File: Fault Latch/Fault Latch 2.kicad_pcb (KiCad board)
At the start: 2 copper layers, 85 x 85 mm, 116 parts, among them J1 1053141312, J3 1053131202, J4 1053131202, J5 1053131202, K3 Fujitsu_FTR-LYCA005x, K5 Fujitsu_FTR-LYCA005x, K6 Fujitsu_FTR-LYCA005x, Q101 Q_NPN_BEC, Q102 Q_NPN_BEC, Q103 Q_NPN_BEC, Q104 Q_NPN_BEC, Q105 Q_NMOS_GSD, Q106 Q_NMOS_GSD, Q110 Q_NPN_BEC, Q111 Q_NPN_BEC, Q112 Q_NMOS_GSD, Q113 Q_NMOS_GSD, Q114 Q_NMOS_GSD, Q115 Q_NMOS_GSD, Q117 Q_NMOS_GSD, Q118 Q_NMOS_GSD, Q119 Q_NMOS_GSD, Q120 Q_NMOS_GSD, Q121 Q_NMOS_GSD, Q122 Q_NMOS_GSD, Q123 Q_NMOS_GSD, Q124 Q_NMOS_GSD, Q125 Q_NMOS_GSD, SW101 SW_Omron_B3FS, SW102 SW_Omron_B3FS, SW103 SW_Omron_B3FS, U1 74LS279, U104 74AHC1G00, U109 74AHC1G00, U112 74AHC1G00, U117 74AHC1G00, U118 LM555xM, U2 LM1117DT-5.0, U3 TestPoint, U7 SN74AHC1G08DBVR, U8 SN74AHC1G08DBVR

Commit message: Fault Latch Finished Schematic V4
Finished revised schematic and started on layout.
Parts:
- removed C102, C119, C120: 100n, Capacitor_SMD:C_0603_1608Metric_Pad1.08x0.95mm_HandSolder
- removed C110: 0.1u, Capacitor_SMD:C_0402_1005Metric
- removed J3, J5: 1053131202, Connector_Molex:Molex_Nano-Fit_105313-xx02_1x02_P2.50mm_Horizontal
- removed K5, K6: Fujitsu_FTR-LYCA005x, Relay_THT:Relay_SPDT_Fujitsu_FTR-LYCA005x_FormC_Vertical
- removed Q119, Q121, Q122, Q123, Q124, Q125: Q_NMOS_GSD, Package_TO_SOT_SMD:SOT-23
- removed R106, R107, R109, R116, R126, R134: 1k, Resistor_SMD:R_1210_3225Metric
- removed R131: 15k, Resistor_SMD:R_1210_3225Metric
- removed R135: 510R, Resistor_SMD:R_1210_3225Metric
- removed R138, R139, R140: 10k, Resistor_SMD:R_1210_3225Metric
- removed U104, U109, U112, U117: 74AHC1G00, Package_TO_SOT_SMD:SOT-23-5
- added C1: 100n, Capacitor_SMD:C_0603_1608Metric_Pad1.08x0.95mm_HandSolder, F.Cu at (224.7, 89.4)
- added C2: 0.1u, Capacitor_SMD:C_0402_1005Metric, F.Cu at (228.8, 64.5)
- added C3: 0.1u, Capacitor_SMD:C_0402_1005Metric, F.Cu at (228.8, 72.7)
- added C4: 1u, Capacitor_SMD:C_0402_1005Metric, F.Cu at (270.2, 30.7)
- added C5: 0.1u, Capacitor_SMD:C_0402_1005Metric, F.Cu at (270.2, 32.7)
- added C6: 0.1u, Capacitor_SMD:C_0402_1005Metric, F.Cu at (270.2, 34.7)
- added D1: TVS Diode, Diode_SMD:Nexperia_DSN1608-2_1.6x0.8mm, F.Cu at (269.6, 52.8)
- added D2: TVS Diode, Diode_SMD:Nexperia_DSN1608-2_1.6x0.8mm, F.Cu at (269.6, 55.1)
- added D3: TVS Diode, Diode_SMD:Nexperia_DSN1608-2_1.6x0.8mm, F.Cu at (269.6, 57.5)
- added IC1: CD4027BE, 1.Custom:DIP794W53P254L1930H508Q16N, F.Cu at (251.8, 53.0)
- added J2: 4pinNanofit, Connector_Molex:Molex_Nano-Fit_105313-xx04_1x04_P2.50mm_Horizontal, F.Cu at (241.7, 78.8)
- added K1: Relay_SPDT_Omron_G2RL-1, Relay_THT:Relay_SPDT_Omron_G2RL-1, F.Cu at (85.5, 53.9)
- added K2: Relay_SPDT_Omron_G2RL-1, Relay_THT:Relay_SPDT_Omron_G2RL-1, F.Cu at (85.5, 77.0)
- added Q3: Q_NMOS_GSD, Package_TO_SOT_SMD:SOT-23, F.Cu at (243.3, 67.3)
- added Q4: Q_NMOS_GSD, Package_TO_SOT_SMD:SOT-23, F.Cu at (243.3, 71.9)
- added R1: 10k, Resistor_SMD:R_1210_3225Metric, F.Cu at (249.1, 31.8)
- added R10: 510R, Resistor_SMD:R_1210_3225Metric, F.Cu at (266.0, 31.8)
- added R12: 10k, Resistor_SMD:R_1210_3225Metric, F.Cu at (248.6, 67.0)
- added R13: 510R, Resistor_SMD:R_1210_3225Metric, F.Cu at (248.6, 71.2)
- added R141: 5.6k, Resistor_SMD:R_1210_3225Metric, F.Cu at (266.0, 40.3)
- added R2: 1k, Resistor_SMD:R_1210_3225Metric, F.Cu at (249.1, 36.0)
- added R3: 270R, Resistor_SMD:R_1210_3225Metric, F.Cu at (249.1, 40.3)
- added R4: 10k, Resistor_SMD:R_1210_3225Metric, F.Cu at (254.8, 31.8)
- added R5: 2.2k, Resistor_SMD:R_1210_3225Metric, F.Cu at (254.8, 36.0)
- added R6: 1k, Resistor_SMD:R_1210_3225Metric, F.Cu at (254.8, 40.3)
- added R7: 10k, Resistor_SMD:R_1210_3225Metric, F.Cu at (260.4, 31.8)
- added R8: 1k, Resistor_SMD:R_1210_3225Metric, F.Cu at (260.4, 36.0)
- added R9: 10k, Resistor_SMD:R_1210_3225Metric, F.Cu at (260.4, 40.3)
- added TP5: TestPoint, TestPoint:TestPoint_Pad_D1.5mm, F.Cu at (254.9, 77.8)
- added TP8: TestPoint, TestPoint:TestPoint_Pad_D1.5mm, F.Cu at (254.9, 81.4)
- added TP9: TestPoint, TestPoint:TestPoint_Pad_D1.5mm, F.Cu at (254.9, 84.9)
- added U4: 74HC00, Package_DIP:DIP-14_W7.62mm, F.Cu at (231.7, 32.0)
- added U5: SFH617A-1, Package_DIP:DIP-4_W7.62mm, F.Cu at (258.9, 51.0)
- added U6: SFH617A-1, Package_DIP:DIP-4_W7.62mm, F.Cu at (258.9, 57.7)
- H101, H102, H103, H104: footprint MountingHole:MountingHole_3.2mm_M3 -> MountingHole:MountingHole_4.3mm_M4
- J1: footprint footprints:CONN_SD-105314-100_12_MOL -> 1.Custom:CONN_SD-105314-100_12_MOL_Nano
- K3: value Fujitsu_FTR-LYCA005x -> Relay_SPDT_Omron_G2RL-1; footprint Relay_THT:Relay_SPDT_Fujitsu_FTR-LYCA005x_FormC_Vertical -> Relay_THT:Relay_SPDT_Omron_G2RL-1
- U1: footprint Package_SO:SOIC-16_3.9x9.9mm_P1.27mm -> Package_DIP:DIP-16_W7.62mm
- U3: value TestPoint -> SFH617A-1; footprint TestPoint:TestPoint_Pad_D1.5mm -> Package_DIP:DIP-4_W7.62mm
- moved H103 321.4 mm to (382.4, 139.7)
- moved H101 238.1 mm to (382.1, 72.8)
- moved H102 236.6 mm to (310.3, 137.7)
- moved R101 205.1 mm to (-47.5, -2.59), turned to 0 degrees
- moved R105 198.9 mm to (-47.5, 1.62), turned to 0 degrees
- moved R111 192.8 mm to (-47.5, 26.9), turned to 0 degrees
- moved R108 192.8 mm to (-47.5, 14.2), turned to 0 degrees
- moved R110 192.4 mm to (-47.5, 22.7), turned to 0 degrees
- moved SW101 183.6 mm to (-12.3, -31.2), turned to 0 degrees
- moved U3 180.9 mm to (258.9, 44.4), turned to 0 degrees
- moved Q102 172.4 mm to (-19.8, 2.33)
- moved Q101 169.5 mm to (-19.8, -2.30), turned to 0 degrees
- moved H104 164.5 mm to (312.6, 71.7)
- moved TP11 163.5 mm to (239.0, 54.6)
- moved TP4 158.9 mm to (235.5, 51.1)
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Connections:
- net Net-(D109-K) renamed /BSPD_SR
- net Net-(R101-Pad1) renamed /BMS Button -
- net Net-(R113-Pad1) renamed /IMD Button -
- net Net-(R122-Pad1) renamed /BSPD Button -
- D104 pad 1: +5V -> +12V
- D108 pad 1: +5V -> +12V
- D110 pad 1: +5V -> +12V
- J1 pad 1: /BMS Light Out -> GND
- J1 pad 10: /BSPD_HV -> /IMD Light -
- J1 pad 11: /IMD_HV -> unconnected-(J1-Pad11)
- J1 pad 12: /NBMS_HV -> /Shutdown Circuit Out
- J1 pad 2: /BMS Light In -> /BMS
- J1 pad 3: /TSSI Green Out -> /TSSI Red -
- J1 pad 4: /TSSI Green In -> /BMS Light -
- J1 pad 5: /IMD Light Out -> /BSPD Light -
- J1 pad 6: /IMD Light In -> /Shutdown Circuit In
- J1 pad 7: /TSSI Red Out -> /12V Isolated +
- J1 pad 8: +12V -> /IMD
- J1 pad 9: unconnected-(J1-Pad9) -> /TSSI Green -
- J4 pad 1: /Shutdown Circuit In -> /BSPD
- J4 pad 2: /Shutdown Circuit Out -> unconnected-(J4-Pad2)
- K3 pad 11: Net-(K3-Pad11) -> /Shutdown Circuit Out
- K3 pad 12: GND -> unconnected-(K3-Pad12)
- K3 pad 14: /Shutdown Circuit In -> Net-(K2-Pad11)
- K3 pad A1: +5V -> +12V
- K3 pad A2: Net-(D104-A) -> Net-(D110-A)
- Q106 pad 3: /IMD Light Out -> Net-(Q106-D)
- Q115 pad 3: /BMS Light Out -> Net-(Q115-D)
- R112 pad 1: +12V -> /IMD Light -
- R112 pad 2: /IMD Light In -> Net-(Q106-D)
- TP11 pad 1: Net-(K5-Pad11) -> Net-(K2-Pad11)
- TP4 pad 1: Net-(K3-Pad11) -> Net-(K1-Pad11)
- U118 pad 3: /CLOCK -> Net-(IC1-CLOCK1)
- U3 pad 1: +12V -> /BSPD
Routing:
- net +5V: track 380.7 -> 0.00 mm, vias 3 -> 0
- net +12V: track 216.1 -> 0.00 mm, vias 4 -> 0
- net /BSPD_HV: track 133.0 -> 0.00 mm, vias 1 -> 0
- net /IMD_HV: track 109.7 -> 0.00 mm, vias 1 -> 0
- net /NBMS_HV: track 86.2 -> 0.00 mm, vias 1 -> 0
- net /BMS_SR: track 72.4 -> 0.00 mm, vias 5 -> 0
- net /IMD_SR: track 63.0 -> 0.00 mm, vias 7 -> 0
- net /Shutdown Circuit In: track 53.4 -> 0.00 mm
- net /NRESET_BMS: track 39.9 -> 0.00 mm, vias 2 -> 0
- net /BSPD_SR: track 39.5 -> 0.00 mm, vias 3 -> 0
- net /NIMD_LV: track 38.5 -> 0.00 mm, vias 4 -> 0
- net /NBMS_LV: track 37.2 -> 0.00 mm, vias 5 -> 0
- net /NBPSD_LV: track 32.4 -> 0.00 mm, vias 3 -> 0
- net /NRESET_IMD: track 30.8 -> 0.00 mm
- net /BMS Light In: track 30.0 -> 0.00 mm, vias 1 -> 0
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- removed copper zone on F.Cu, net +12V
- removed copper zone on B.Cu, net GND
- removed copper zone on F.Cu, net GND
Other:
- board outline removed
- board text removed: "BMS_FAULT"
- board text removed: "BMS_RESET"
- board text removed: "BSPD_FAULT"
- board text removed: "BSPD_RESET"
- board text removed: "IMD_FAULT"
- board text removed: "IMD_RESET"

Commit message: Fault Latch V4 (almost RTO needs mounting holes)
Needs a final edge cut and mounting holes placed on it, besides that everything else is ready.
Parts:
- added R150: 270R, Resistor_SMD:R_1210_3225Metric, F.Cu at (79.6, 110.8)
- C101, C105, C106, C107, C108, C112, C114, C115, Q101, Q102, Q103, Q104, Q110, Q111, R101, R105, R108, R110, R111, R113, R114, R115, R119, R120, R122, R123, R124, R127, R129: moved to B.Cu
- D1, D2, D3: value TVS Diode -> Bi-TVS Diode; footprint Diode_SMD:Nexperia_DSN1608-2_1.6x0.8mm -> Diode_SMD:D_SOD-523
- R5: footprint Resistor_SMD:R_1210_3225Metric -> Resistor_SMD:R_2512_6332Metric
- moved C4 222.7 mm to (61.0, 107.0), turned to 180 degrees
- moved C5 220.1 mm to (63.0, 107.0)
- moved R141 213.5 mm to (68.2, 120.8)
- moved IC1 203.1 mm to (59.3, 117.6)
- moved R10 194.1 mm to (92.8, 119.5), turned to 90 degrees
- moved TP11 184.0 mm to (56.4, 77.0)
- moved D1 182.3 mm to (99.9, 119.4), turned to 90 degrees
- moved J2 181.8 mm to (61.7, 104.0), turned to 180 degrees
- moved D2 180.1 mm to (99.9, 115.6), turned to 90 degrees
- moved TP4 179.5 mm to (56.4, 63.2)
- moved TP6 178.3 mm to (61.2, 92.2)
- moved U7 176.8 mm to (66.5, 110.8)
- moved R13 171.1 mm to (84.8, 120.5), turned to 90 degrees
- moved R2 170.1 mm to (94.9, 107.8)
- moved U5 169.6 mm to (99.1, 107.8), turned to 90 degrees
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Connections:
- D1 pad 1: /BMS -> GND
- D1 pad 2: GND -> /BMS
- D2 pad 1: /IMD -> GND
- D2 pad 2: GND -> /IMD
- D3 pad 1: /BSPD -> GND
- D3 pad 2: GND -> /BSPD
- J1 pad 11: unconnected-(J1-Pad11) -> /BSPD Light -
- J1 pad 12: /Shutdown Circuit Out -> /BMS
- J1 pad 2: /BMS -> /Shutdown Circuit In
- J1 pad 5: /BSPD Light - -> unconnected-(J1-Pad5)
- J1 pad 6: /Shutdown Circuit In -> /IMD
- J1 pad 7: /12V Isolated + -> +12V
- J1 pad 8: /IMD -> /Shutdown Circuit Out
- J2 pad 1: /5V FL -> +5V
- J4 pad 1: /BSPD -> unconnected-(J4-Pad1)
- J4 pad 2: unconnected-(J4-Pad2) -> /BSPD
- Q112 pad 3: /TSSI Green Out -> Net-(Q112-D)
- Q113 pad 3: /TSSI Red Out -> Net-(Q113-D)
- R130 pad 1: /TSSI Green In -> Net-(Q112-D)
- R130 pad 2: +12V -> /TSSI Green -
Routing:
- net +5V: track 0.00 -> 405.3 mm, vias 0 -> 19
- net +12V: track 0.00 -> 173.5 mm, vias 0 -> 6
- net /Shutdown Circuit In: track 0.00 -> 131.4 mm, vias 0 -> 2
- net /Shutdown Circuit Out: track 0.00 -> 122.2 mm, vias 0 -> 1
- net /BMS_SR: track 0.00 -> 95.7 mm, vias 0 -> 5
- net /NBPSD_LV: track 0.00 -> 91.9 mm, vias 0 -> 5
- net /IMD_SR: track 0.00 -> 75.8 mm, vias 0 -> 4
- net /NIMD_LV: track 0.00 -> 73.4 mm, vias 0 -> 1
- net Net-(U1C-~{S}-Pad11): track 0.00 -> 73.2 mm, vias 0 -> 2
- net /BSPD_SR: track 0.00 -> 68.2 mm, vias 0 -> 7
- net /NBMS_LV: track 0.00 -> 63.0 mm, vias 0 -> 1
- net /BMS Button -: track 0.00 -> 56.1 mm, vias 0 -> 1
- net /NRESET_BMS: track 0.00 -> 53.6 mm, vias 0 -> 1
- net Net-(U1B-~{S}): track 0.00 -> 46.9 mm, vias 0 -> 2
- net Net-(U1A-~{S}-Pad2): track 0.00 -> 45.8 mm
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- added copper zone on B.Cu, net GND
- added copper zone on F.Cu, net GND
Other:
- board outline added: 85 x 85 mm
- board text added: "FAULT LATCH V4"
- board text removed: "FAULT LATCH V3"

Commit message: Fault Latch RTO V4
Ready to order might push a different one with more sketches for final order.
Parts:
- H101, H102, H103, H104: footprint MountingHole:MountingHole_4.3mm_M4 -> MountingHole:MountingHole_4.3mm_M4_DIN965_Pad_TopOnly
- moved H101 173.0 mm to (50.6, 46.6)
- moved G*** 159.6 mm to (69.2, 132.1)
- moved H104 143.2 mm to (50.6, 131.6)
- moved H103 101.2 mm to (127.2, 131.6)
- moved G*** 87.3 mm to (124.4, 58.4), turned to -90 degrees
- moved G*** 86.3 mm to (125.8, 66.6), turned to -90 degrees
- moved H102 57.0 mm to (127.2, 46.6)
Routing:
- net +5V: track 405.3 -> 404.1 mm
- net +12V: track 173.5 -> 172.8 mm
- net GND: vias 230 -> 238
- net (no net): vias 0 -> 1
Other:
- board size 85 x 85 mm -> 85.8 x 94.2 mm

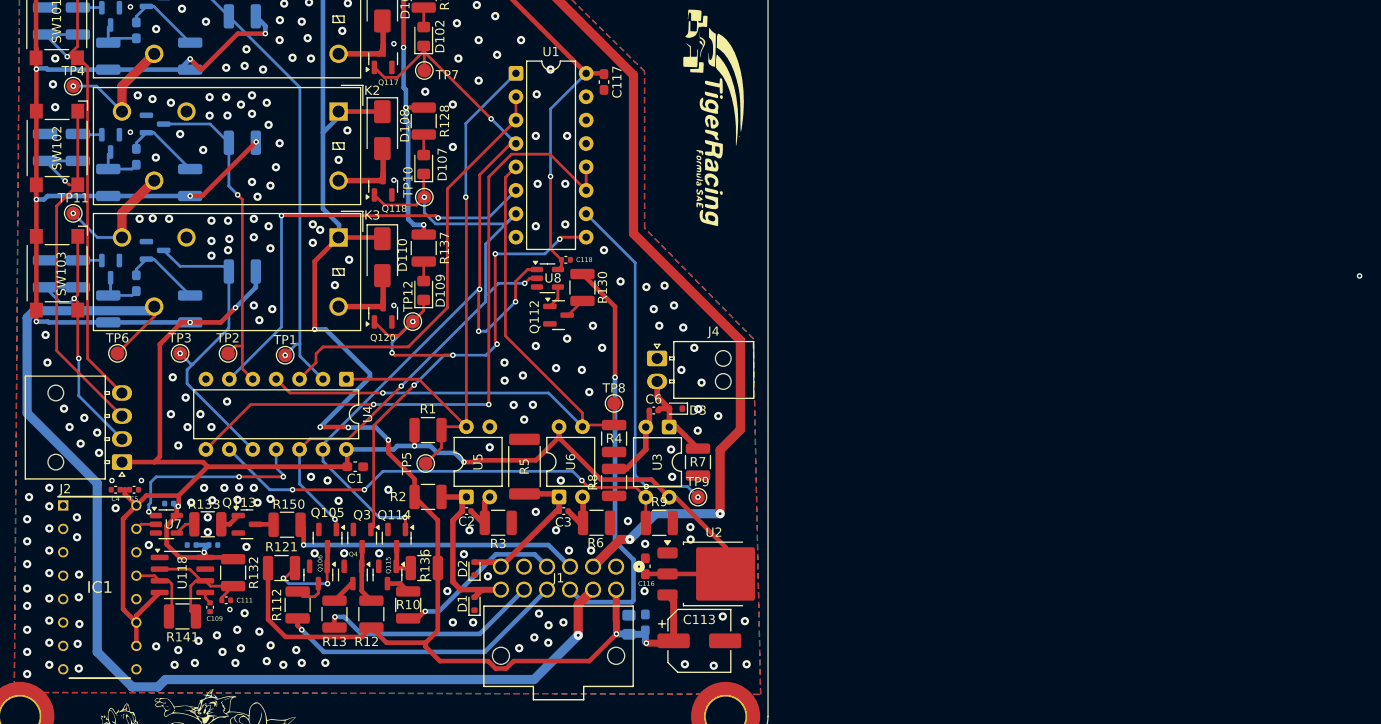
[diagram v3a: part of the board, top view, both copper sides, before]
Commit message: Minor Ground Revision FL V4
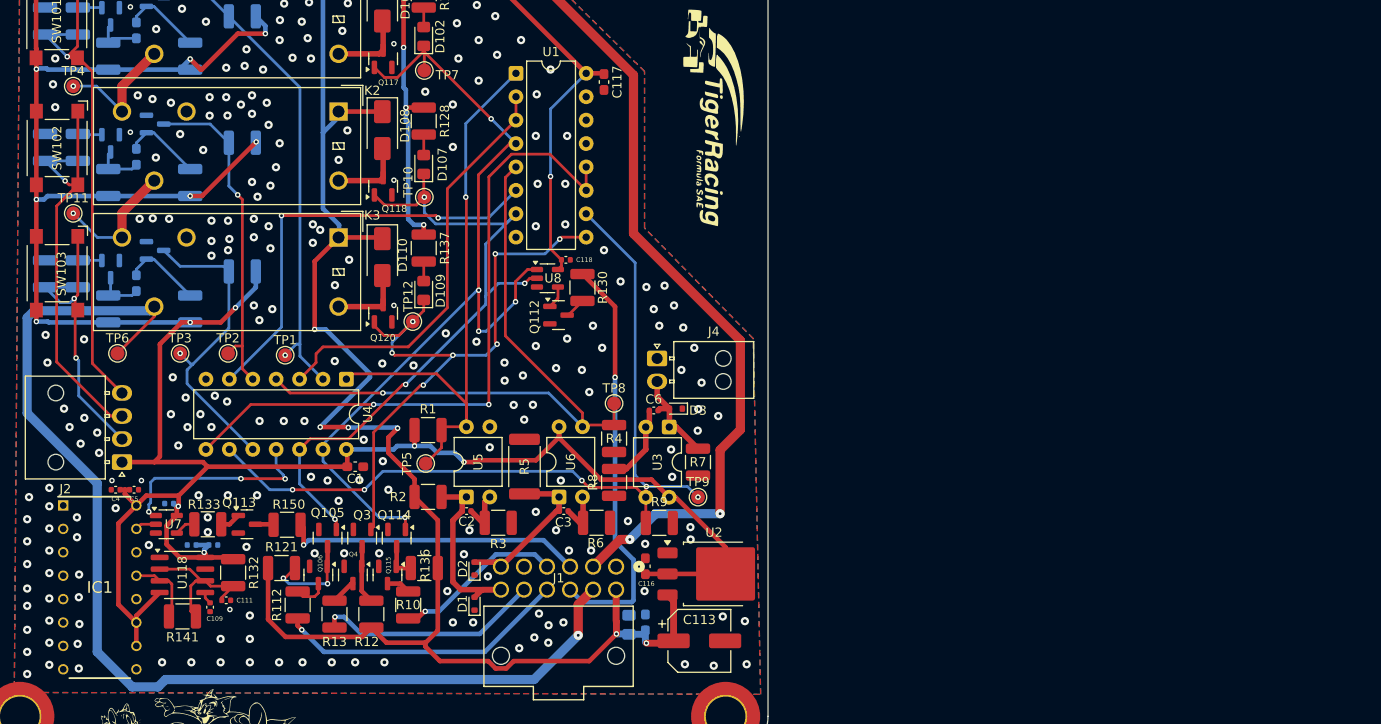
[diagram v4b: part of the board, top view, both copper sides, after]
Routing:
- net +12V: track 172.8 -> 174.9 mm
- net /NBMS_LV: track 63.0 -> 65.0 mm
- net /IMD Button -: track 44.7 -> 45.4 mm
- net GND: vias 238 -> 239
- net (no net): vias 1 -> 0

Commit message: Final RTO Fault Latch V4
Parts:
- added G***: LOGO, LOGO, F.Cu at (115.0, 47.3)
- moved G*** 39.8 mm to (86.1, 47.4), turned to 0 degrees
- moved G*** 37.6 mm to (94.3, 46.0), turned to 0 degrees

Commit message: FINAL RTO FL V4
Added tables for I/O and fixed some traces
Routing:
- net GND: vias 239 -> 278
